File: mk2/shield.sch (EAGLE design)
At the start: 49 parts, among them P0 CON_DIL_20, P1 CON_DIL_20, P2 CON_DIL_20, P3 CON_DIL_20, P4 CON_DIL_20, P5 CON_DIL_20

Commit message: [mega88 led ctrl]
	- add atmega88 controller for interface leds
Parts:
- added U$5: ATMEGA88, mega88:ATMEGA88
- added U$6: CON_DIL_3, connector:CON_DIL_3
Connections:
- new net MISO_LED: MISO.C, U$5.SDA/ADC4/PCINT12
- new net MOSI_LED: MOSI.C, U$5.SCL/ADC5/PCINT13
- new net MOSI_MEGA1284: DRAGON.P$6, EXT0.P$6, U$1.MOSI/ICP3/PCINT13, U$3.MOSI/ICP3/PCINT13, U$5.T1/OC0B/PCINT21, U$6.P$1
- new net MOSI_MEGA88: U$5.MOSI/OC2A/PCINT3, U$6.P$3
- new net RX0_LED: RX0.C, U$5.ADC2/PCINT10
- new net RX1_LED: RX1.C, U$5.XTAL2
- new net SDA_LED: SDA.C, U$5.ADC3/PCINT11
- new net TX0_LED: TX0.C, U$5.ADC1/PCINT9
- new net TX1_LED: TX1.C, U$5.XTAL1
- new net VCC_MEGA1284: JP1.P$1, R13.1, U$1.AREF, U$1.AVCC, U$1.VCC@0, U$1.VCC@1, U$1.VCC@2, U$3.AREF, U$3.AVCC, U$3.VCC@0, U$3.VCC@1, U$3.VCC@2
- net /RESET: now also U$5.RESET
- net GND: now also U$5.GND@0, U$5.GND@1, U$5.GND@3
- net MISO: now also U$5.AIN0/OC0A/PCINT22, U$5.MISO/PCINT4; no longer MISO.C
- net MOSI: now also U$6.P$2; no longer DRAGON.P$6, EXT0.P$6, MOSI.C, U$1.MOSI/ICP3/PCINT13, U$3.MOSI/ICP3/PCINT13
- net RX0: now also U$5.XCK/PCINT20; no longer RX0.C
- net RX1: now also U$5.INT0/PCINT18; no longer RX1.C
- net SCK: now also U$5.SCK/PCINT5
- net SDA: now also U$5.RXD/PCINT16; no longer SDA.C
- net TX0: now also U$5.INT1/OC2B/PCINT19; no longer TX0.C
- net TX1: now also U$5.TX/PCINT17; no longer TX1.C
- net VCC: now also U$5.AREF, U$5.AVCC, U$5.VCC@0, U$5.VCC@1; no longer JP1.P$1, R13.1, U$1.AREF, U$1.AVCC, U$1.VCC@0, U$1.VCC@1, U$1.VCC@2, U$3.AREF, U$3.AVCC, U$3.VCC@0, U$3.VCC@1, U$3.VCC@2
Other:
- moved on the sheet: MISO, MOSI, R10, R2, R3, R4, R5, R6, R7, R8, R9, RX0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

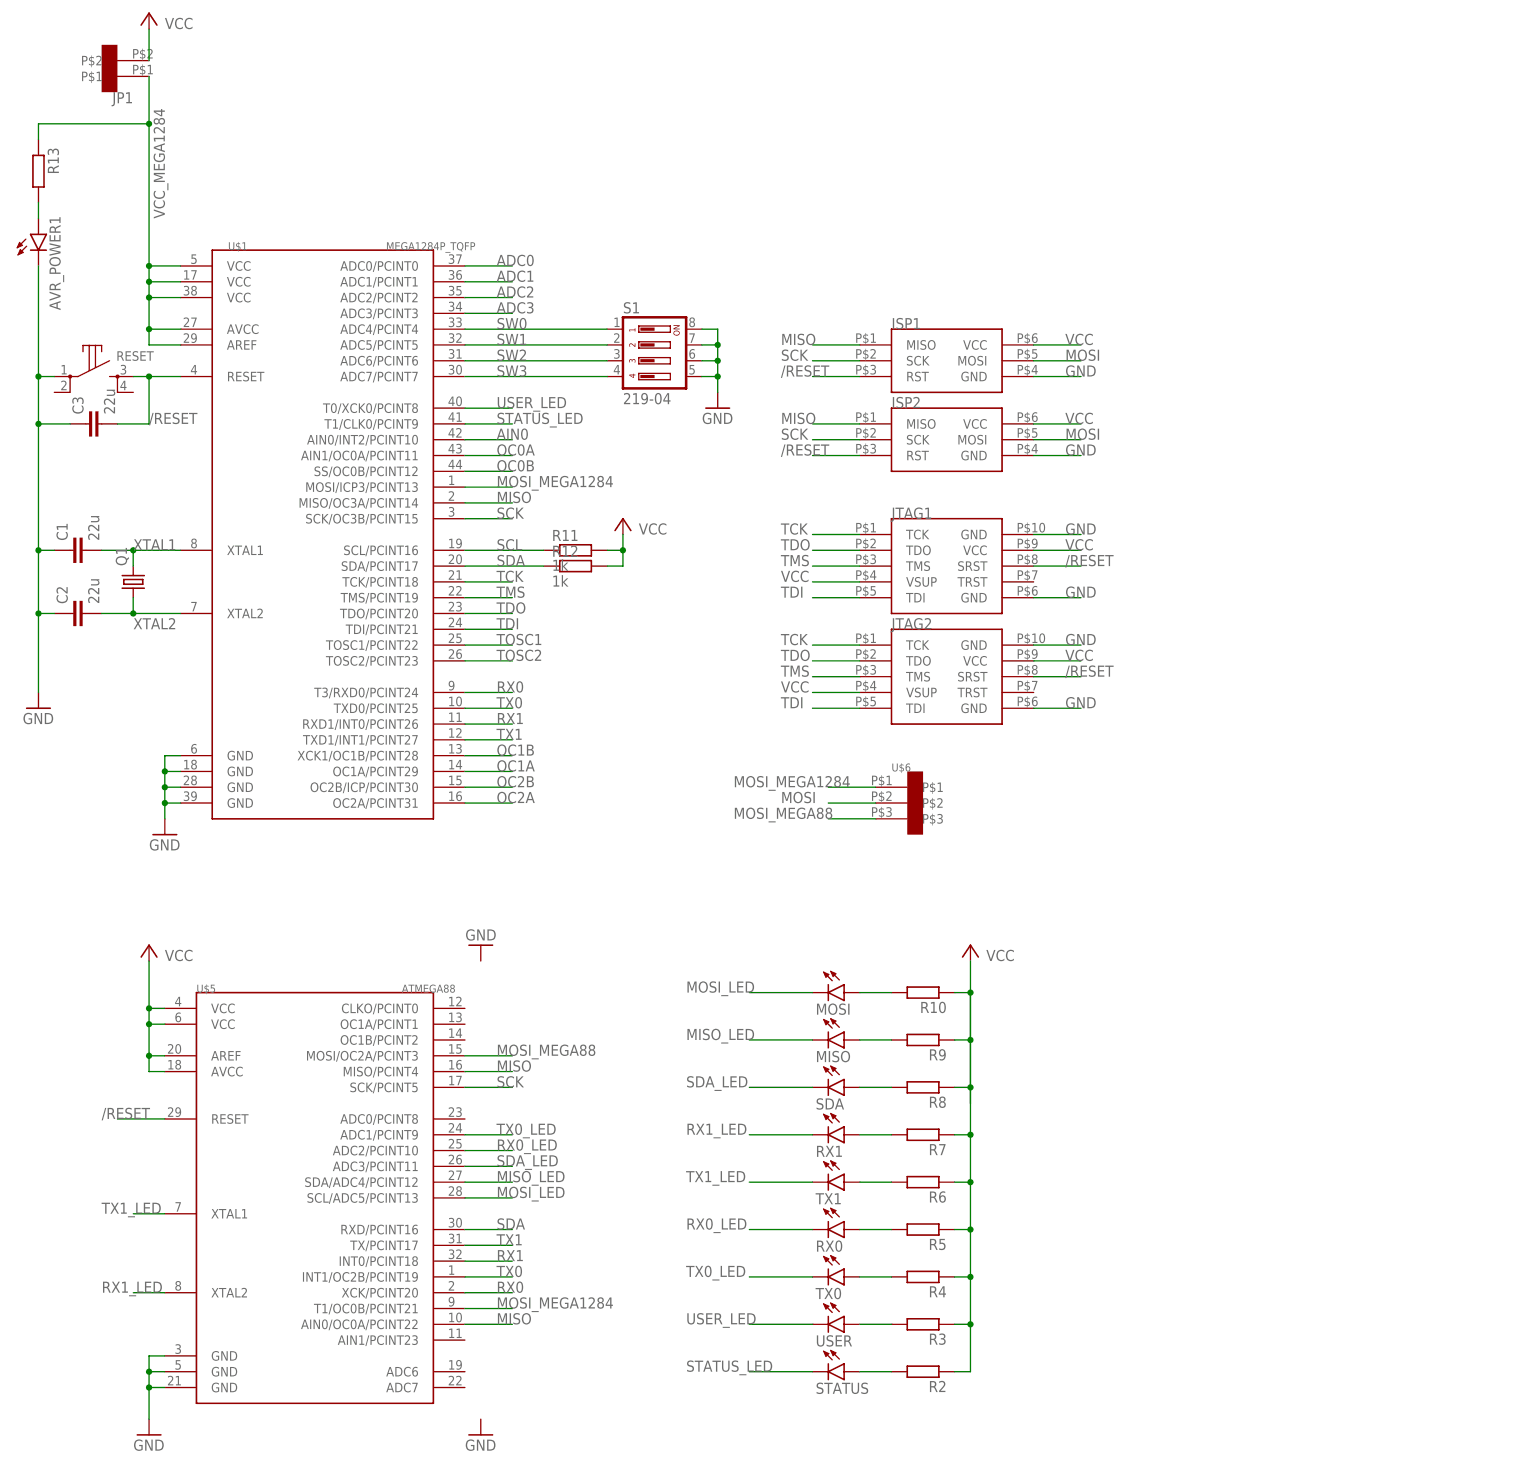
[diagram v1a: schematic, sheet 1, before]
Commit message: [mk2 update part values]
	- update/add values of some parts for mk2 shield and mk2 ftdiusb
	  extension board
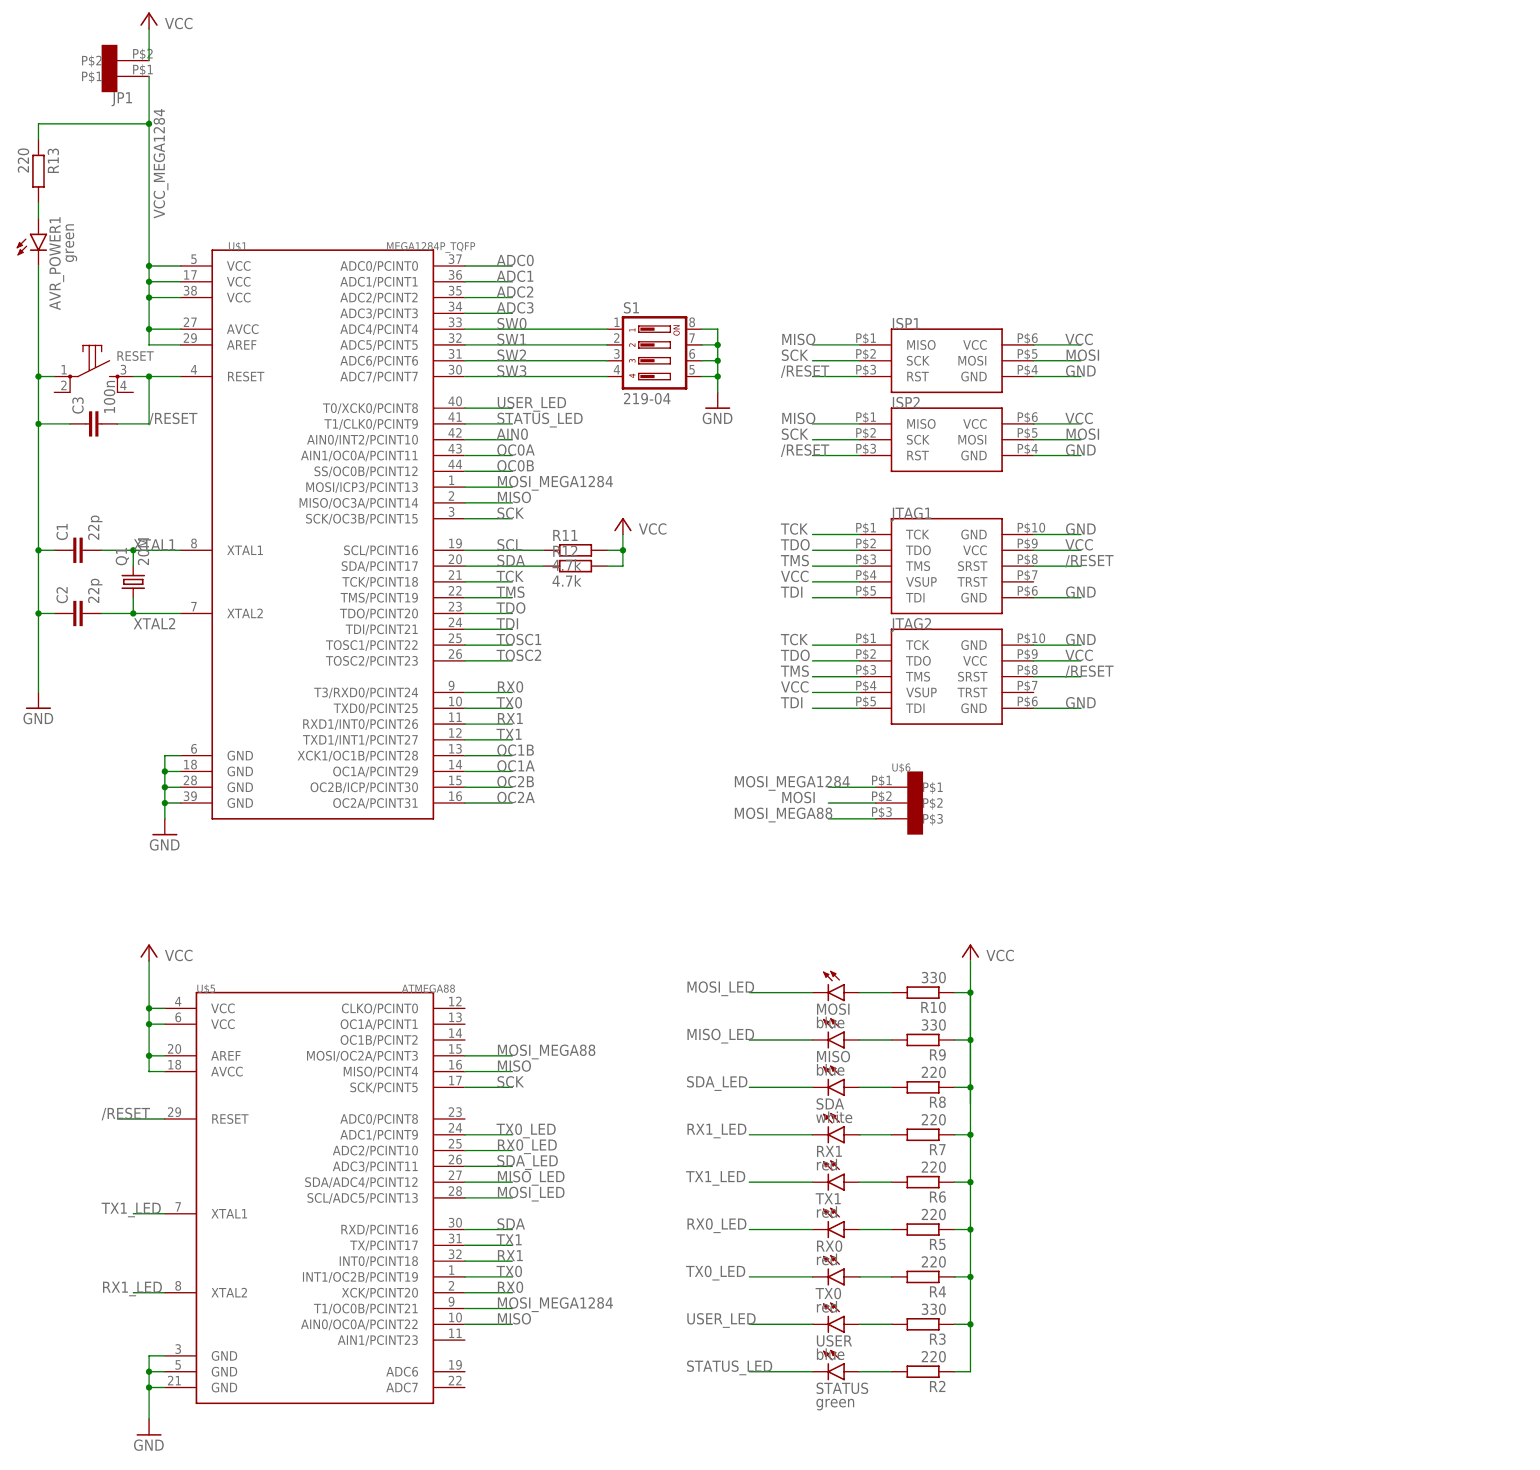
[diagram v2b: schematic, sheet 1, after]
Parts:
- AVR_POWER1, BOARD_POWER, STATUS: value (none) -> green
- C1, C2: value 22u -> 22p
- C3: value 22u -> 100n
- C4: value (none) -> 100u
- MISO, MOSI, USER: value (none) -> blue
- Q1: value (none) -> 20M
- R1, R13, R2, R4, R5, R6, R7, R8: value (none) -> 220
- R10, R3, R9: value (none) -> 330
- R11, R12: value 1k -> 4.7k
- RX0, RX1, TX0, TX1: value (none) -> red
- SDA: value (none) -> white

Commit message: [fix atmega1284p adapter drill size]
	- extend the drill size of the atmega1284p adapter
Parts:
- U$3: device 1284p.rpt:MEGA1284P_ADAPTER -> mega1284p:MEGA1284P_ADAPTER
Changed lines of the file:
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@@
 <part name="R12" library="rcl" library_urn="urn:adsk.eagle:library:334" deviceset="R-EU_" device="R0603" package3d_urn="urn:adsk.eagle:package:23555/3" value="4.7k"/>
 <part name="GND6" library="supply1" library_urn="urn:adsk.eagle:library:371" deviceset="GND" device=""/>
-<part name="U$3" library="1284p.rpt" deviceset="MEGA1284P_ADAPTER" device=""/>
+<part name="U$3" library="mega1284p" deviceset="MEGA1284P_ADAPTER" device=""/>
 <part name="GND7" library="supply1" library_urn="urn:adsk.eagle:library:371" deviceset="GND" device=""/>
 <part name="P+5" library="supply1" library_urn="urn:adsk.eagle:library:371" deviceset="VCC" device=""/>

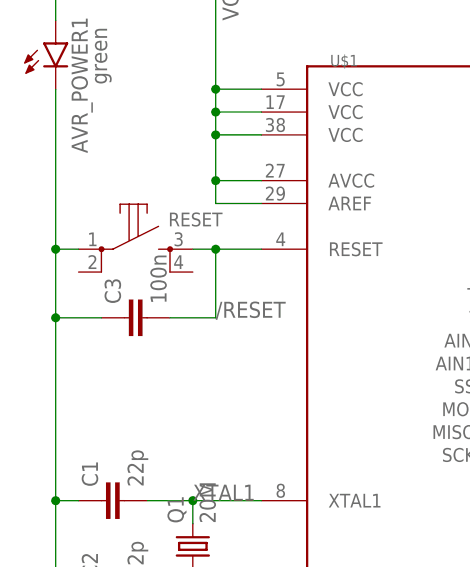
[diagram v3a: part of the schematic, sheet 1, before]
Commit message: [fix mk2 power connector]
	- move the power connector to the dragon board to match the actual
	  position  on the dragon
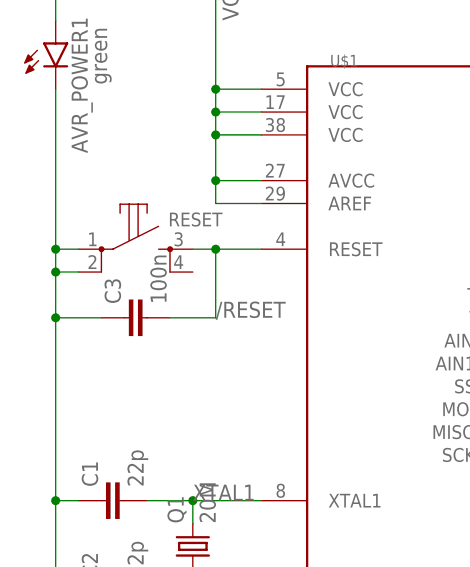
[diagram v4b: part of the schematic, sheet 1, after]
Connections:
- net GND: now also RESET.2
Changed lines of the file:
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@@
 <wire x1="-48.26" y1="106.68" x2="-50.8" y2="106.68" width="0.1524" layer="91"/>
 <junction x="-50.8" y="78.74"/>
-<wire x1="-50.8" y1="106.68" x2="-50.8" y2="99.06" width="0.1524" layer="91"/>
+<wire x1="-50.8" y1="106.68" x2="-50.8" y2="104.14" width="0.1524" layer="91"/>
+<wire x1="-50.8" y1="104.14" x2="-50.8" y2="99.06" width="0.1524" layer="91"/>
 <wire x1="-50.8" y1="99.06" x2="-50.8" y2="78.74" width="0.1524" layer="91"/>
 <pinref part="C3" gate="G$1" pin="1"/>
@@
 <wire x1="-50.8" y1="124.46" x2="-50.8" y2="106.68" width="0.1524" layer="91"/>
 <junction x="-50.8" y="106.68"/>
+<pinref part="RESET" gate="G$1" pin="2"/>
+<wire x1="-48.26" y1="104.14" x2="-50.8" y2="104.14" width="0.1524" layer="91"/>
+<junction x="-50.8" y="104.14"/>
 </segment>
 <segment>

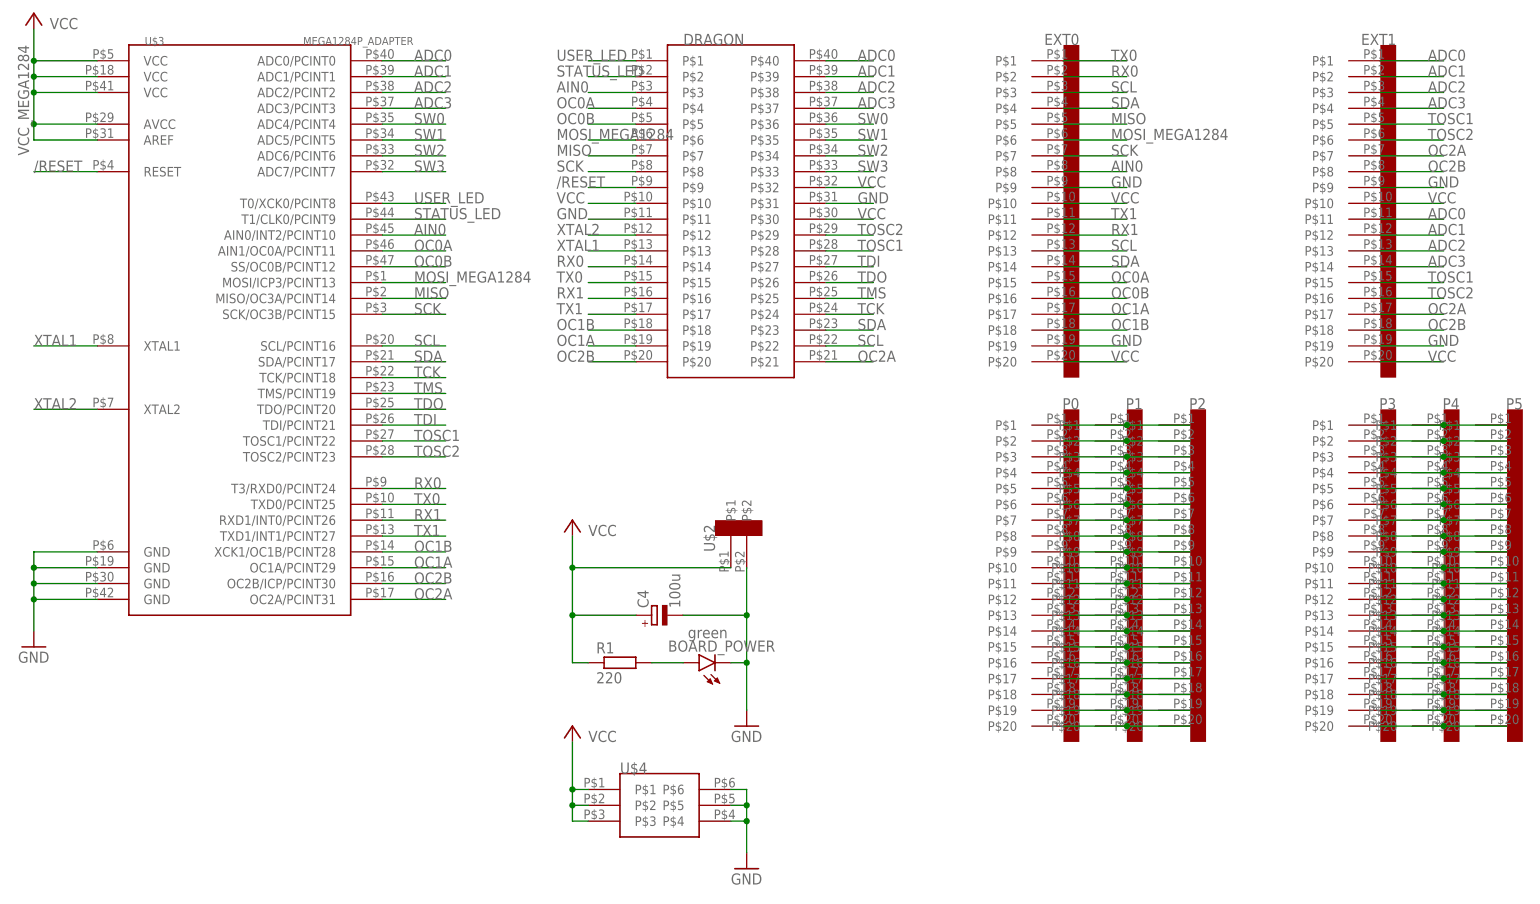
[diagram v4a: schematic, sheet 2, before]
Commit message: [mk2 reset separation]
	- split the jtag and isp connectors such that
		- isp is connected to the atmega88 and the external isp
		- jtat is connected to the atmega1284 and the external jtag
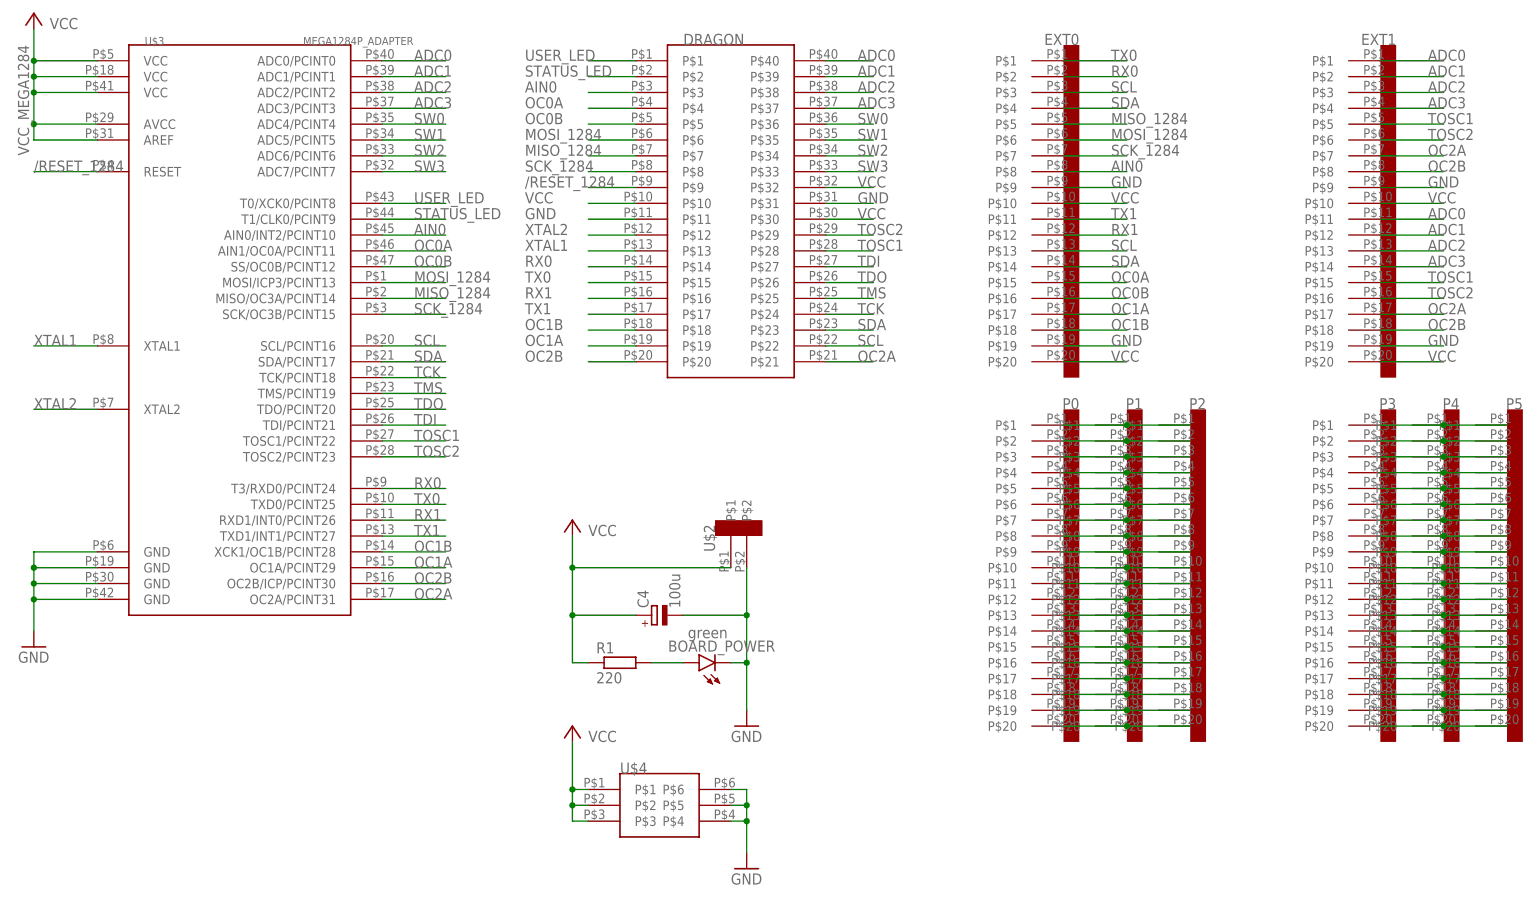
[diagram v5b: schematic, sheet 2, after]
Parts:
- renumbered ISP1 to ISP1_DRAGON, ISP2 to ISP2_EXT
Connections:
- net MOSI_MEGA88 renamed MOSI_88
- removed net /RESET: C3.2, DRAGON.P$9, ISP1_DRAGON.RST, ISP2_EXT.RST, JTAG1.SRST, JTAG2.SRST, RESET.3, U$1.RESET, U$3.RESET, U$5.RESET
- removed net MISO: DRAGON.P$7, EXT0.P$5, ISP1_DRAGON.MISO, ISP2_EXT.MISO, U$1.MISO/OC3A/PCINT14, U$3.MISO/OC3A/PCINT14, U$5.AIN0/OC0A/PCINT22, U$5.MISO/PCINT4
- removed net MOSI: ISP1_DRAGON.MOSI, ISP2_EXT.MOSI, U$6.P$2
- removed net MOSI_MEGA1284: DRAGON.P$6, EXT0.P$6, U$1.MOSI/ICP3/PCINT13, U$3.MOSI/ICP3/PCINT13, U$5.T1/OC0B/PCINT21, U$6.P$1
- removed net SCK: DRAGON.P$8, EXT0.P$7, ISP1_DRAGON.SCK, ISP2_EXT.SCK, U$1.SCK/OC3B/PCINT15, U$3.SCK/OC3B/PCINT15, U$5.SCK/PCINT5
- new net /RESET_1284: C3.2, DRAGON.P$9, JTAG1.SRST, JTAG2.SRST, RESET.3, U$1.RESET, U$3.RESET
- new net /RESET_88: ISP1_DRAGON.RST, ISP2_EXT.RST, U$5.RESET
- new net MISO_1284: DRAGON.P$7, EXT0.P$5, U$1.MISO/OC3A/PCINT14, U$3.MISO/OC3A/PCINT14, U$5.AIN0/OC0A/PCINT22
- new net MISO_88: ISP1_DRAGON.MISO, ISP2_EXT.MISO, U$5.MISO/PCINT4
- new net MOSI_1284: DRAGON.P$6, EXT0.P$6, U$1.MOSI/ICP3/PCINT13, U$3.MOSI/ICP3/PCINT13, U$5.T1/OC0B/PCINT21
- new net MOSI_DRAGON: ISP1_DRAGON.MOSI, U$6.P$2
- new net MOSI_EXT: ISP2_EXT.MOSI, U$6.P$1
- new net SCK_1284: DRAGON.P$8, EXT0.P$7, U$1.SCK/OC3B/PCINT15, U$3.SCK/OC3B/PCINT15
- new net SCK_88: ISP1_DRAGON.SCK, ISP2_EXT.SCK, U$5.SCK/PCINT5
